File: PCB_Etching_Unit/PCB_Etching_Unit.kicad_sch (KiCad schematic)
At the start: 91 parts, among them M1 Motor_DC, M2 Motor_DC, Q1 TIP42, Q10 TIP42, Q11 TIP41, Q12 2N3904, Q13 TIP42, Q14 BC558, Q15 BC558, Q16 BC558, Q17 BC558, Q18 BC558, Q19 BC558, Q2 TIP42, Q20 BC558, Q3 TIP42, Q4 TIP42, Q5 TIP42, Q6 TIP41, Q7 TIP41, Q8 TIP42, Q9 TIP41, SW1 SW_MEC_5G, SW2 SW_MEC_5G, SW3 SW_MEC_5G, SW4 SW_MEC_5G, SW5 SW_MEC_5G, SW6 SW_MEC_5G, SW7 SW_MEC_5G, U1 HDSP-7801, U11 4511, U2 HDSP-7801, U3 HDSP-7801, U4 HDSP-7801, U5 4027, U6 4027, U9 4011

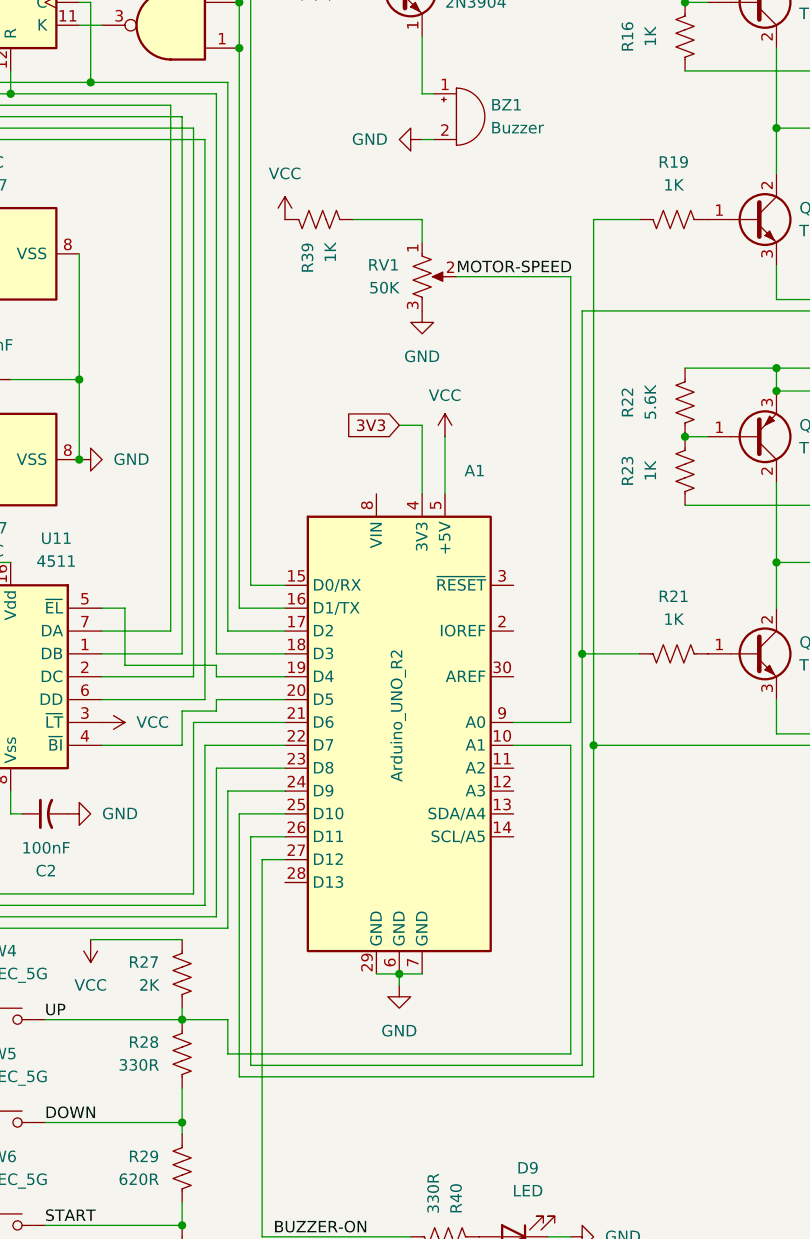
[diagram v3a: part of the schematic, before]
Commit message: Starting on PCB layout and added assembly, pcb production link in readme
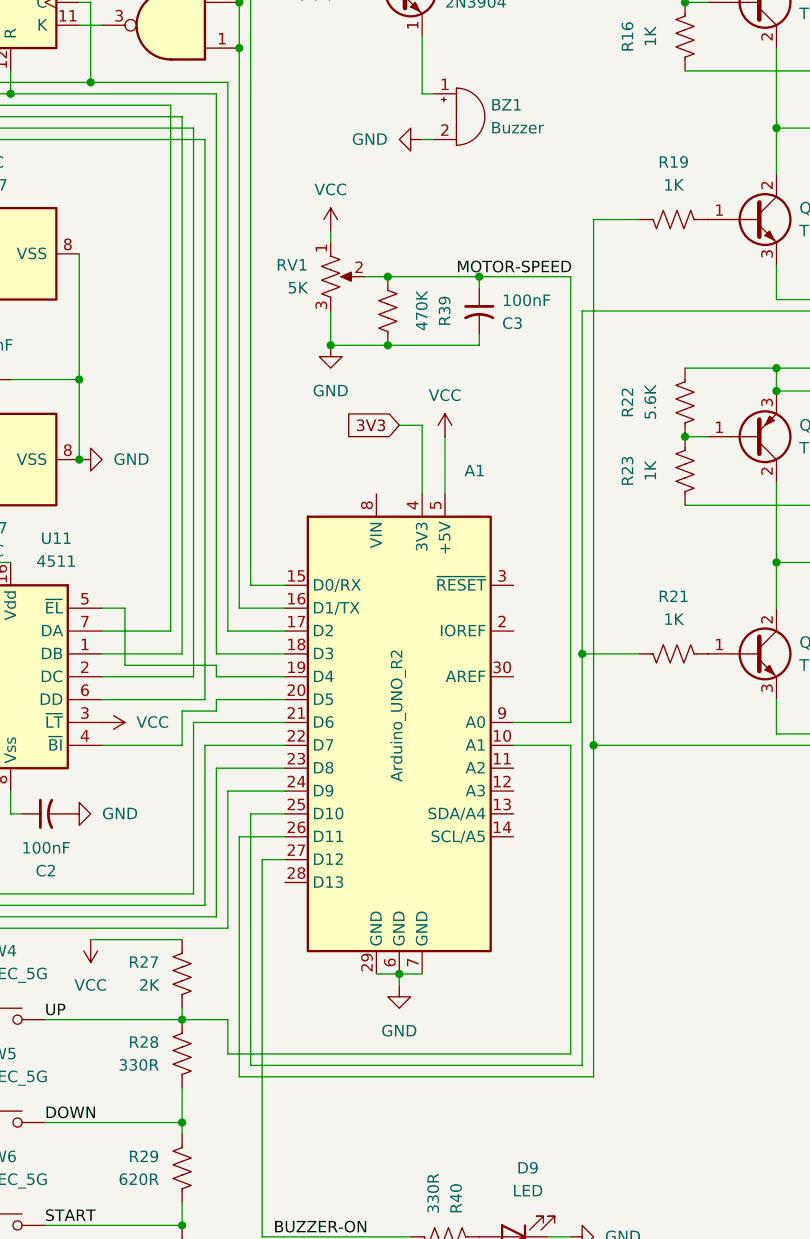
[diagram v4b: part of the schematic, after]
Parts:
- added C3: 100nF, Capacitor_THT:C_Disc_D9.0mm_W5.0mm_P5.00mm, symbol Device:C_Small_US
- A1: footprint Module:Arduino_UNO_R2 -> Module:Arduino_UNO_R2_WithMountingHoles
- BZ1: footprint Buzzer_Beeper:Buzzer_12x9.5RM7.6 -> Connector_PinHeader_2.54mm:PinHeader_1x02_P2.54mm_Vertical
- C1, C2: footprint (none) -> Capacitor_THT:C_Disc_D9.0mm_W5.0mm_P5.00mm
- Q1, Q13, Q2, Q3: footprint Package_TO_SOT_THT:TO-220-3_Horizontal_TabDown -> Package_TO_SOT_THT:TO-220-3_Vertical
- R39: value 1K -> 470K
- RV1: value 50K -> 5K; footprint Potentiometer_SMD:Potentiometer_Bourns_3214G_Horizontal -> Potentiometer_THT:Potentiometer_Piher_T-16H_Single_Horizontal
- SW1, SW2, SW3, SW4, SW5, SW6, SW7: footprint Button_Switch_SMD:SW_MEC_5GSH9 -> Button_Switch_THT:SW_TH_Tactile_Omron_B3F-106x
- U11, U6: footprint (none) -> Package_DIP:DIP-16_W7.62mm
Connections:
- net GND: now also R39.2, C3.2
- net MOTOR-SPEED: now also R39.1, C3.1
- net VCC: now also RV1.1; no longer R39.2
- net at R19.2, R26.2: now also A1.26 (D11); no longer A1.25 (D10)
- net at R20.2, R21.2: now also A1.25 (D10); no longer A1.26 (D11)
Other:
- moved on the sheet: RV1
